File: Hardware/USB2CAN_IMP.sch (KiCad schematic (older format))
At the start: 24 parts, among them U6 STM32F042C6Tx, U7 MCP2551-I-SN, Y3 16 MHz

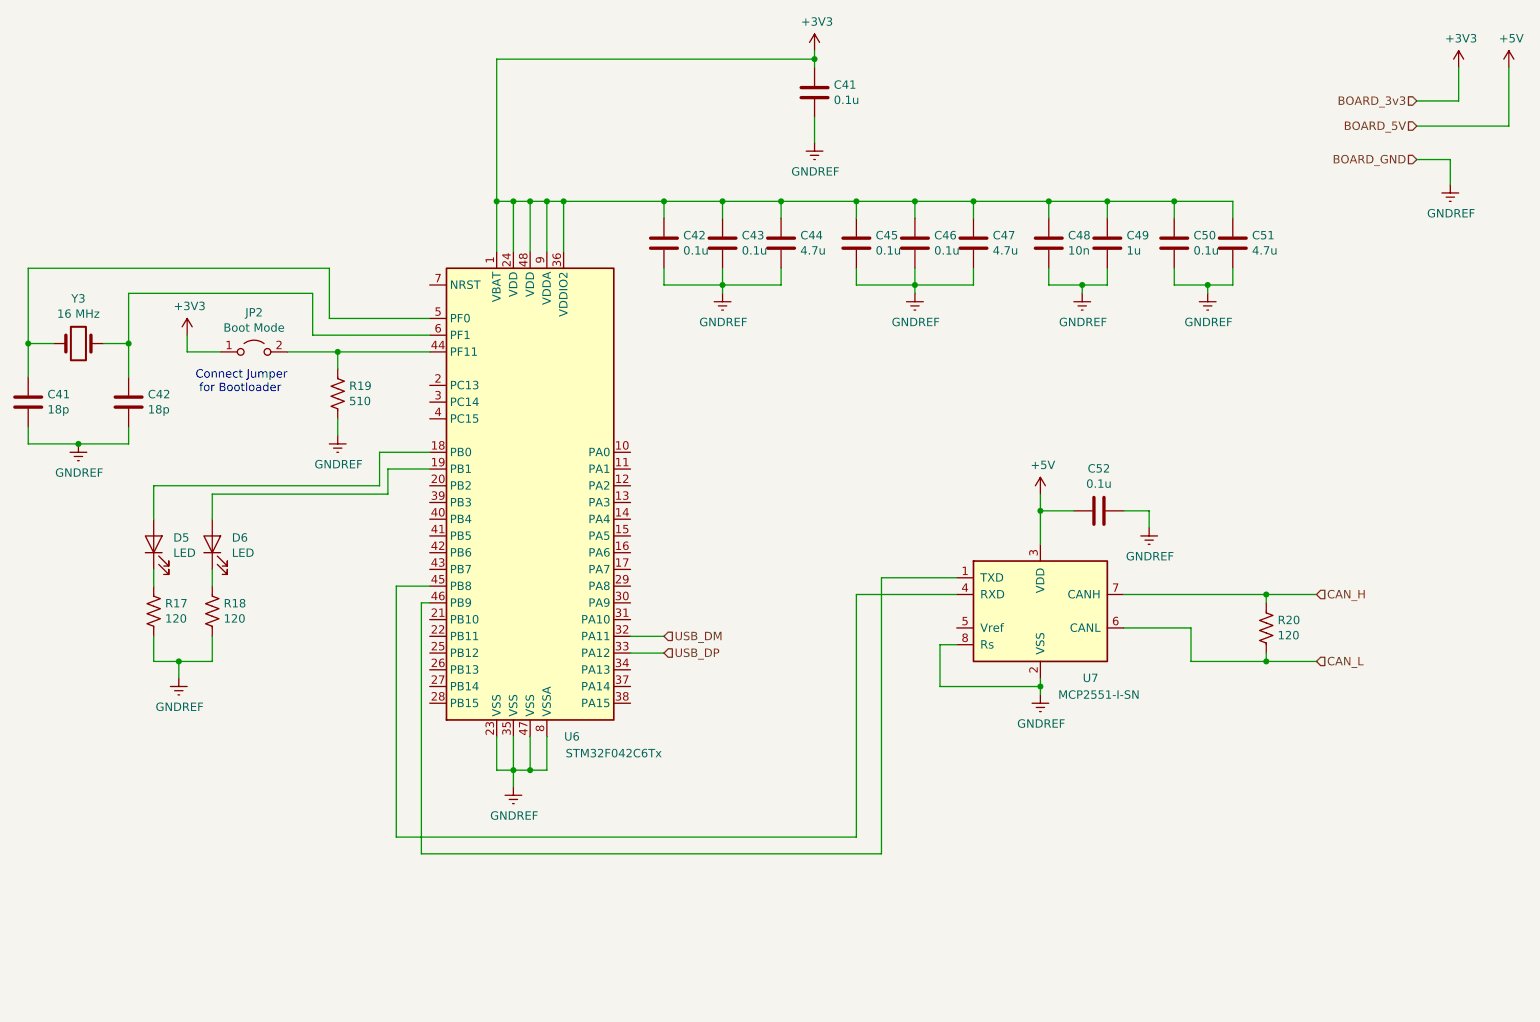
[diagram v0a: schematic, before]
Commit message: Added footprints to schematic symbols
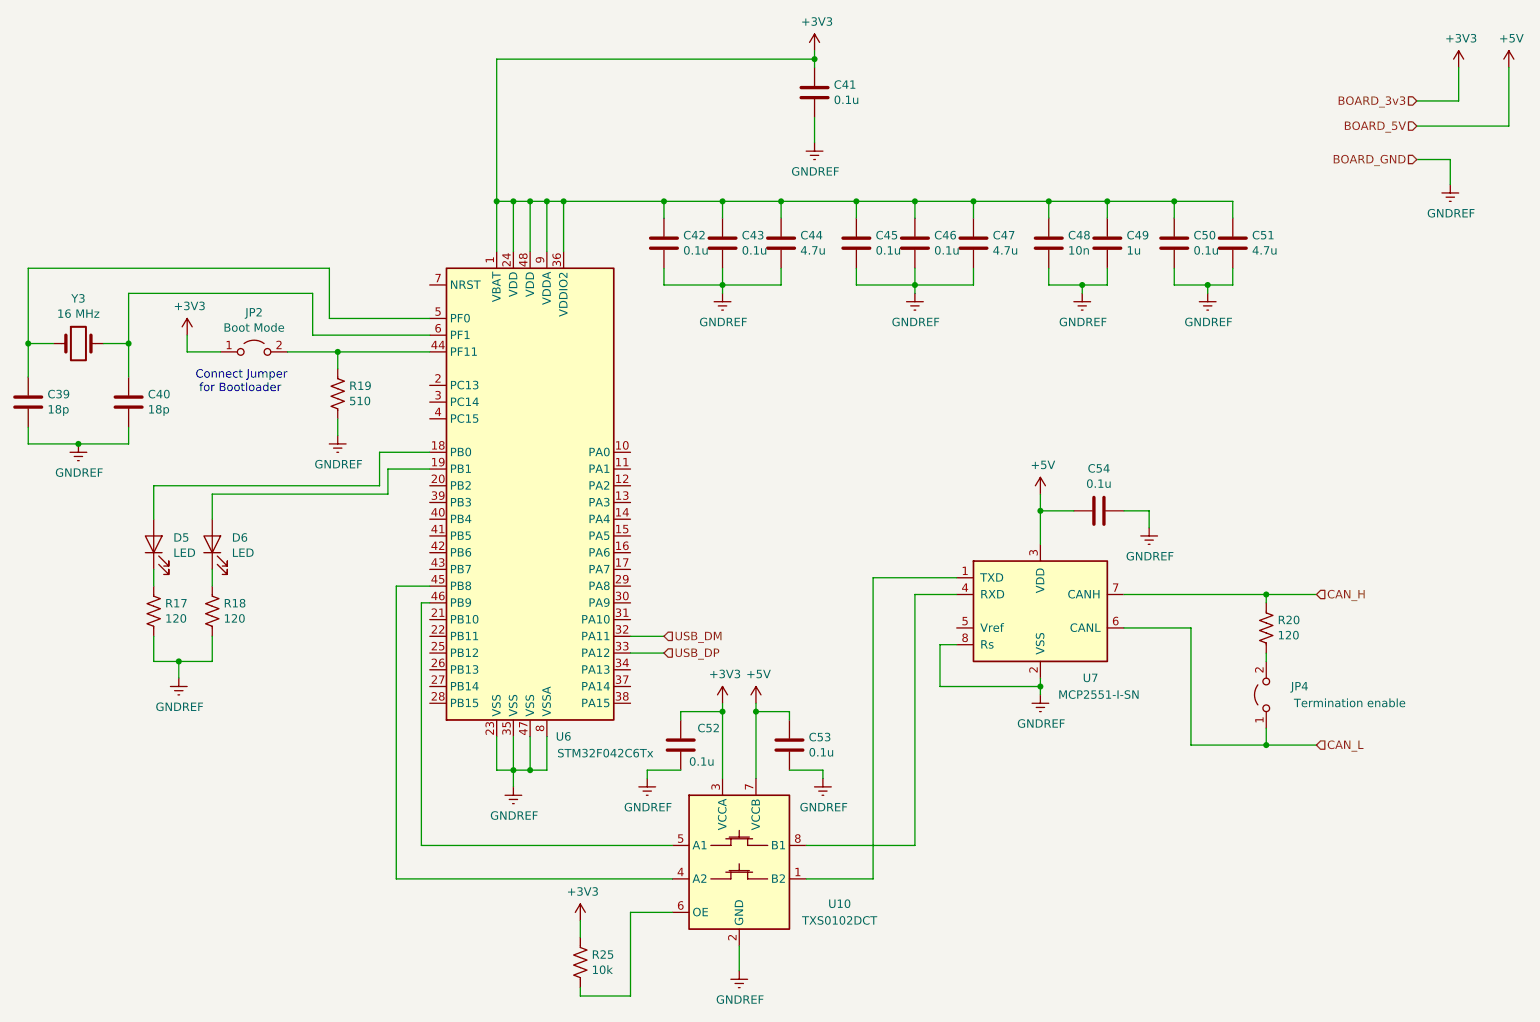
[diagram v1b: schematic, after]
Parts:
- added C52, C53: 0.1u, Capacitor_SMD:C_0603_1608Metric, symbol Device:C
- added JP4: Termination enable, Connector_PinHeader_1.27mm:PinHeader_2x01_P1.27mm_Vertical_SMD, symbol Jumper:Jumper_2_Open
- added R25: 10k, Resistor_SMD:R_1206_3216Metric, symbol Device:R_US
- added U10: TXS0102DCT, Package_SO:SSOP-8_2.95x2.8mm_P0.65mm, symbol Logic_LevelTranslator:TXS0102DCT
- C39: renamed from C41; footprint (none) -> Capacitor_SMD:C_0603_1608Metric
- C40: renamed from C42; footprint (none) -> Capacitor_SMD:C_0603_1608Metric
- C41, C42, C43, C44, C45, C46, C47, C48, C49, C50, C51: footprint (none) -> Capacitor_SMD:C_0603_1608Metric
- C54: renamed from C52; footprint (none) -> Capacitor_SMD:C_0603_1608Metric
- D5, D6: footprint (none) -> LED_SMD:LED_0805_2012Metric_Castellated
- JP2: footprint (none) -> Connector_PinHeader_1.27mm:PinHeader_2x01_P1.27mm_Vertical_SMD
- R17, R18, R19, R20: footprint (none) -> Resistor_SMD:R_1206_3216Metric
- Y3: footprint (none) -> Crystal:Crystal_SMD_2016-4Pin_2.0x1.6mm
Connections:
- net +3V3: now also C52.1, R25.1, U10.3 (VCCA)
- net +5V: now also C53.1, U10.7 (VCCB)
- net CAN_L: now also JP4.1 (A); no longer R20.2
- net GNDREF: now also C52.2, C53.2, U10.2 (GND)
- net at U7.4 (RXD): now also U10.8 (B1); no longer U6.45 (PB8)
- net at U7.1 (TXD): now also U10.1 (B2); no longer U6.46 (PB9)
- new net: JP4.2 (B), R20.2
- new net: U10.4 (A2), U6.45 (PB8)
- new net: U10.5 (A1), U6.46 (PB9)
- new net: R25.2, U10.6 (OE)
